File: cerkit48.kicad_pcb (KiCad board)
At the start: 2 copper layers, 237.3 x 84.9 mm, 103 parts, among them J1 I2C, SW10 CherryMX, SW11 CherryMX, SW12 CherryMX, SW13 CherryMX, SW14 CherryMX, SW15 CherryMX, SW16 CherryMX, SW17 CherryMX, SW18 CherryMX, SW19 CherryMX, SW2 CherryMX, SW20 CherryMX, SW21 CherryMX, SW22 CherryMX, SW23 CherryMX, SW24 CherryMX, SW25 CherryMX, SW26 CherryMX, SW27 CherryMX, SW28 CherryMX, SW29 CherryMX, SW3 CherryMX, SW30 CherryMX, SW31 CherryMX, SW32 CherryMX, SW33 CherryMX, SW34 CherryMX, SW35 CherryMX, SW36 CherryMX, SW37 CherryMX, SW38 CherryMX, SW39 CherryMX, SW4 CherryMX, SW40 CherryMX, SW41 CherryMX, SW42 CherryMX, SW43 CherryMX, SW44 CherryMX, SW45 CherryMX, SW46 CherryMX, SW47 CherryMX, SW48 CherryMX, SW49 CherryMX, SW5 CherryMX, SW6 CherryMX, SW7 CherryMX, SW8 CherryMX, SW9 CherryMX, U1 proton_c

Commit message: rounded the edges of the board
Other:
- board size 237.3 x 84.9 mm -> 235.7 x 83.3 mm

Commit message: rounded the edges of the PCB
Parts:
- moved J1 0.48 mm to (208.3, 54.5)
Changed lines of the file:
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@@
   (layers
     (0 F.Cu signal)
-    (31 B.Cu signal)
+    (31 B.Cu signal hide)
     (32 B.Adhes user hide)
     (33 F.Adhes user hide)
@@
     (35 F.Paste user hide)
     (36 B.SilkS user hide)
-    (37 F.SilkS user hide)
+    (37 F.SilkS user)
     (38 B.Mask user hide)
     (39 F.Mask user hide)
@@
   )
   (module cerkit48:PIN_HEADER_I2C (layer F.Cu)
-    (at 208.28 53.975 270)
+    (at 208.28 54.45125 270)
     (fp_text reference J1 (at 0 0.5 90) (layer F.SilkS)
       (effects (font (size 1 1) (thickness 0.15)))
@@
     (polygon
       (pts
-        (xy 259.55625 134.9375) (xy 23.8125 134.9375) (xy 23.8125 51.59375) (xy 259.55625 50.8)
+        (xy 259.55625 134.9375) (xy 23.8125 134.9375) (xy 23.8125 51.59375) (xy 259.55625 51.59375)
       )
     )

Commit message: modified gerber files
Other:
- net class Default: trace_width 0.25 -> 0.254
- net class Power added: clearance 0.2, trace_width 0.381, via_dia 0.8, via_drill 0.4
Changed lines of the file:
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@@
     (thickness 1.6)
     (drawings 92)
-    (tracks 384)
+    (tracks 385)
     (zones 0)
     (modules 103)
@@
   (layers
     (0 F.Cu signal)
-    (31 B.Cu signal hide)
+    (31 B.Cu signal)
     (32 B.Adhes user hide)
     (33 F.Adhes user hide)
@@
   )
   (setup
-    (last_trace_width 0.25)
+    (last_trace_width 0.254)
     (trace_clearance 0.2)
     (zone_clearance 0.508)
@@
   (net_class Default "This is the default net class."
     (clearance 0.2)
-    (trace_width 0.25)
+    (trace_width 0.254)
     (via_dia 0.8)
     (via_drill 0.4)
     (uvia_dia 0.3)
     (uvia_drill 0.1)
-    (add_net 3.3V)
     (add_net COL0)
     (add_net COL1)
@@
     (add_net COL8)
     (add_net COL9)
-    (add_net GND)
     (add_net "Net-(D1-Pad2)")
     (add_net "Net-(D10-Pad2)")
@@
     (add_net SDA)
   )
+  (net_class Power ""
+    (clearance 0.2)
+    (trace_width 0.381)
+    (via_dia 0.8)
+    (via_drill 0.4)
+    (uvia_dia 0.3)
+    (uvia_drill 0.1)
+    (add_net 3.3V)
+    (add_net GND)
+  )
   (module MountingHole:MountingHole_3.2mm_M3 (layer F.Cu)
     (at 256.54 54.61 180)
@@
   (segment (start 199.920001 111.020001) (end 199.920001 53.444999) (width 0.25) (layer B.Cu) (net 54))
   (segment (start 202.565 113.665) (end 199.920001 111.020001) (width 0.25) (layer B.Cu) (net 54))
-  (segment (start 202.460001 101.833997) (end 201.422 102.871998) (width 0.25) (layer B.Cu) (net 55))
-  (segment (start 202.460001 94.705999) (end 202.460001 101.833997) (width 0.25) (layer B.Cu) (net 55))
-  (segment (start 201.682499 93.928497) (end 202.460001 94.705999) (width 0.25) (layer B.Cu) (net 55))
-  (segment (start 203.2 52.705) (end 201.682499 54.222501) (width 0.25) (layer B.Cu) (net 55))
-  (segment (start 201.682499 54.222501) (end 201.682499 93.928497) (width 0.25) (layer B.Cu) (net 55))
-  (segment (start 201.422 102.871998) (end 201.422 107.442) (width 0.25) (layer B.Cu) (net 55))
   (segment (start 201.422 107.442) (end 201.422 107.442) (width 0.25) (layer B.Cu) (net 55))
   (via (at 201.422 107.442) (size 0.8) (drill 0.4) (layers F.Cu B.Cu) (net 55))
   (segment (start 203.322 107.442) (end 206.365 110.485) (width 0.25) (layer F.Cu) (net 55))
   (segment (start 201.422 107.442) (end 203.322 107.442) (width 0.25) (layer F.Cu) (net 55))
+  (segment (start 202.525501 94.674559) (end 202.525501 95.924499) (width 0.381) (layer B.Cu) (net 55))
+  (segment (start 201.616999 93.766057) (end 202.525501 94.674559) (width 0.381) (layer B.Cu) (net 55))
+  (segment (start 203.2 53.18125) (end 201.616999 54.764251) (width 0.381) (layer B.Cu) (net 55))
+  (segment (start 201.616999 54.764251) (end 201.616999 93.766057) (width 0.381) (layer B.Cu) (net 55))
+  (segment (start 201.616999 107.247001) (end 201.422 107.442) (width 0.381) (layer B.Cu) (net 55))
+  (segment (start 201.616999 96.833001) (end 201.616999 107.247001) (width 0.381) (layer B.Cu) (net 55))
+  (segment (start 202.525501 95.924499) (end 201.616999 96.833001) (width 0.381) (layer B.Cu) (net 55))
   (segment (start 206.365 95.24) (end 206.375 95.25) (width 0.25) (layer B.Cu) (net 56))
   (segment (start 32.749463 81.75035) (end 32.870936 81.871823) (width 0.25) (layer B.Cu) (net 57))
@@
   (segment (start 242.2525 100.6475) (end 243.100001 101.495001) (width 0.25) (layer B.Cu) (net 68))
   (segment (start 231.765 95.24) (end 231.775 95.25) (width 0.25) (layer F.Cu) (net 73))
-  (zone (net 56) (net_name GND) (layer F.Cu) (hatch edge 0.508)
+  (zone (net 56) (net_name GND) (layer B.Cu) (hatch edge 0.508)
     (connect_pads (clearance 0.508))
     (min_thickness 0.254)
@@
     )
   )
-  (zone (net 56) (net_name GND) (layer B.Cu) (hatch edge 0.508)
+  (zone (net 56) (net_name GND) (layer F.Cu) (hatch edge 0.508)
     (connect_pads (clearance 0.508))
     (min_thickness 0.254)

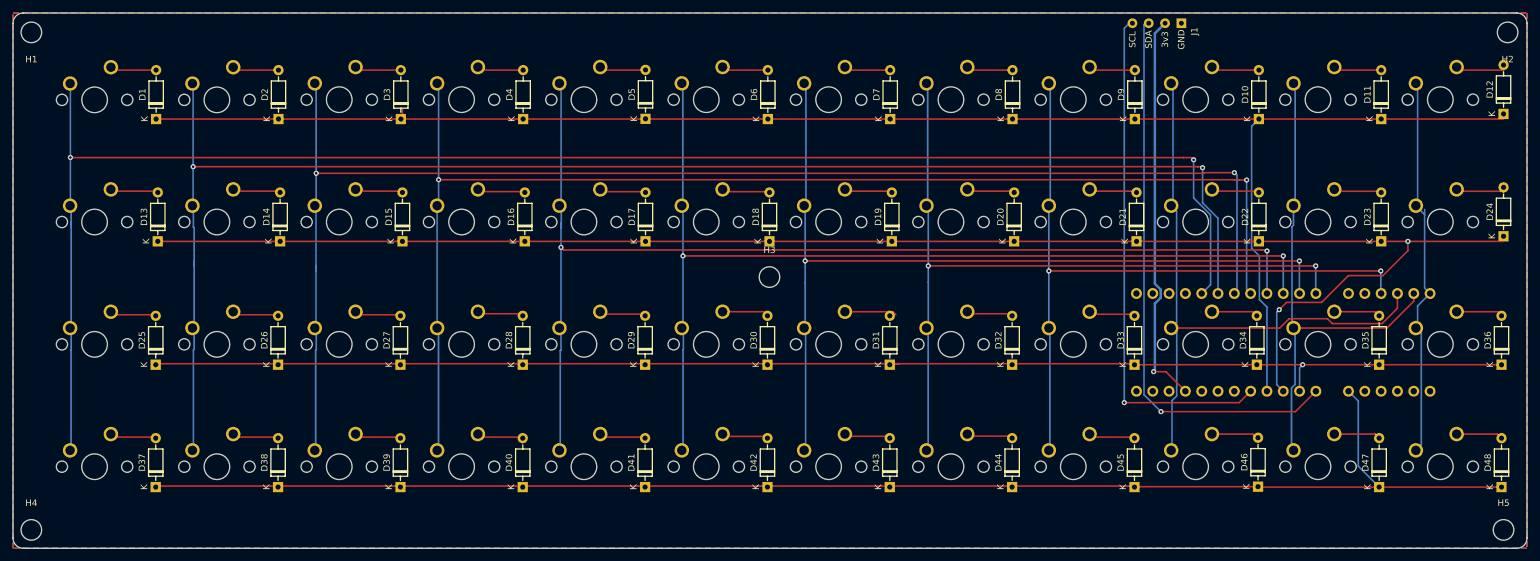
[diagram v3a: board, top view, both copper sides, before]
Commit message: fixed PCB outline
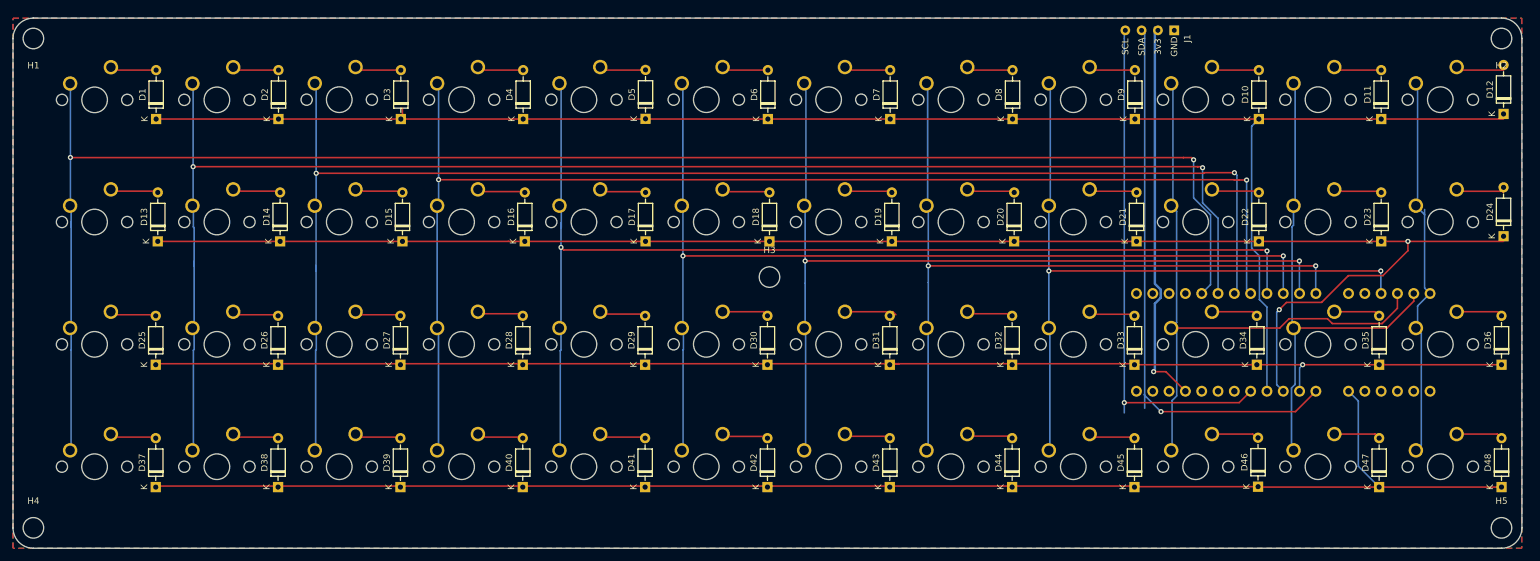
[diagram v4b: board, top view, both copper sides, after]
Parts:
- moved J1 1.57 mm to (207.2, 55.6)
- moved H2 1.35 mm to (255.6, 55.6)
- moved H1 1.00 mm to (27.0, 55.6)
- moved H4 0.45 mm to (27.0, 131.8)
- moved H5 0.45 mm to (255.6, 131.8)
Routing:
- net 3.3V: track 62.0 -> 61.2 mm
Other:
- board size 235.7 x 83.3 mm -> 235 x 82.5 mm

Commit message: centered middle mounting hole
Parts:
- moved D12 1.00 mm to (255.6, 68.3)
- moved H3 1.00 mm to (141.3, 93.7)
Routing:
- net SDA: track 88.2 -> 86.1 mm
- net SCL: track 80.0 -> 78.5 mm
- net 3.3V: track 61.2 -> 62.6 mm
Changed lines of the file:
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@@
     (thickness 1.6)
     (drawings 8)
-    (tracks 387)
+    (tracks 390)
     (zones 0)
     (modules 103)
@@
     (35 F.Paste user hide)
     (36 B.SilkS user)
-    (37 F.SilkS user)
-    (38 B.Mask user)
+    (37 F.SilkS user hide)
+    (38 B.Mask user hide)
     (39 F.Mask user)
     (40 Dwgs.User user)
@@
     (45 Margin user hide)
     (46 B.CrtYd user hide)
-    (47 F.CrtYd user hide)
+    (47 F.CrtYd user)
     (48 B.Fab user hide)
     (49 F.Fab user hide)
@@
   )
   (module Diode_THT:D_DO-35_SOD27_P7.62mm_Horizontal (layer F.Cu)
-    (at 255.905 67.31 90)
+    (at 255.5875 68.2625 90)
     (descr "Diode, DO-35_SOD27 series, Axial, Horizontal, pin pitch=7.62mm, , length*diameter=4*2mm^2, , http://www.diodes.com/_files/packages/DO-35.pdf")
     (tags "Diode DO-35_SOD27 series Axial Horizontal pin pitch 7.62mm  length 4mm diameter 2mm")
@@
   )
   (module MountingHole:MountingHole_3.2mm_M3 (layer F.Cu)
-    (at 141.605 92.71)
+    (at 141.2875 93.6625)
     (descr "Mounting Hole 3.2mm, no annular, M3")
     (tags "mounting hole 3.2mm no annular m3")
@@
   (segment (start 198.755 68.10375) (end 217.805 68.10375) (width 0.25) (layer F.Cu) (net 2))
   (segment (start 217.805 68.10375) (end 236.855 68.10375) (width 0.25) (layer F.Cu) (net 2))
-  (segment (start 236.855 68.10375) (end 255.905 68.10375) (width 0.25) (layer F.Cu) (net 2))
   (segment (start 84.455 68.10375) (end 84.455 66.475652) (width 0.25) (layer F.Cu) (net 2))
   (segment (start 219.065 97.384998) (end 219.065 110.485) (width 0.25) (layer B.Cu) (net 2))
@@
   (segment (start 216.679999 69.228751) (end 216.679999 88.213751) (width 0.25) (layer B.Cu) (net 2))
   (segment (start 217.805 68.10375) (end 216.679999 69.228751) (width 0.25) (layer B.Cu) (net 2))
+  (segment (start 255.42875 68.10375) (end 255.5875 68.2625) (width 0.254) (layer F.Cu) (net 2))
+  (segment (start 236.855 68.10375) (end 255.42875 68.10375) (width 0.254) (layer F.Cu) (net 2))
   (segment (start 58.296875 60.48375) (end 58.208345 60.39522) (width 0.25) (layer F.Cu) (net 3))
   (segment (start 65.405 60.48375) (end 58.296875 60.48375) (width 0.25) (layer F.Cu) (net 3))
@@
   (segment (start 229.91352 60.48375) (end 229.806152 60.376382) (width 0.25) (layer F.Cu) (net 12))
   (segment (start 236.855 60.48375) (end 229.91352 60.48375) (width 0.25) (layer F.Cu) (net 12))
-  (segment (start 255.905 60.48375) (end 249.026559 60.48375) (width 0.25) (layer F.Cu) (net 13))
+  (segment (start 254.9525 60.0075) (end 255.5875 60.6425) (width 0.254) (layer F.Cu) (net 13))
+  (segment (start 248.6025 60.0075) (end 254.9525 60.0075) (width 0.254) (layer F.Cu) (net 13))
   (segment (start 46.153073 79.331823) (end 46.355 79.53375) (width 0.25) (layer F.Cu) (net 14))
   (segment (start 39.220936 79.331823) (end 46.153073 79.331823) (width 0.25) (layer F.Cu) (net 14))
@@
   (segment (start 216.525 110.485) (end 214.742 112.268) (width 0.25) (layer F.Cu) (net 53))
   (segment (start 214.742 112.268) (end 196.85 112.268) (width 0.25) (layer F.Cu) (net 53))
-  (segment (start 196.85 113.8555) (end 196.85 55.5625) (width 0.25) (layer B.Cu) (net 53))
   (via (at 196.85 112.268) (size 0.8) (drill 0.4) (layers F.Cu B.Cu) (net 53))
-  (segment (start 196.85 54.45125) (end 197.00875 54.2925) (width 0.254) (layer B.Cu) (net 53))
-  (segment (start 196.85 55.5625) (end 196.85 54.45125) (width 0.254) (layer B.Cu) (net 53))
-  (via (at 202.565 113.665) (size 0.8) (drill 0.4) (layers F.Cu B.Cu) (net 54))
-  (segment (start 223.505 113.665) (end 226.685 110.485) (width 0.25) (layer F.Cu) (net 54))
+  (segment (start 197.00875 112.10925) (end 196.85 112.268) (width 0.254) (layer B.Cu) (net 53))
+  (segment (start 197.00875 54.2925) (end 197.00875 112.10925) (width 0.254) (layer B.Cu) (net 53))
   (segment (start 202.565 113.665) (end 223.505 113.665) (width 0.25) (layer F.Cu) (net 54))
-  (segment (start 200.025 113.137502) (end 200.025 55.5625) (width 0.25) (layer B.Cu) (net 54))
-  (segment (start 202.565 113.665) (end 199.920001 111.020001) (width 0.25) (layer B.Cu) (net 54))
-  (segment (start 200.025 54.76875) (end 199.54875 54.2925) (width 0.254) (layer B.Cu) (net 54))
-  (segment (start 200.025 55.5625) (end 200.025 54.76875) (width 0.254) (layer B.Cu) (net 54))
+  (segment (start 223.505 113.665) (end 226.685 110.485) (width 0.25) (layer F.Cu) (net 54))
+  (via (at 202.565 113.665) (size 0.8) (drill 0.4) (layers F.Cu B.Cu) (net 54))
+  (segment (start 199.922001 54.665751) (end 199.922001 111.022001) (width 0.254) (layer B.Cu) (net 54))
+  (segment (start 199.54875 54.2925) (end 199.922001 54.665751) (width 0.254) (layer B.Cu) (net 54))
+  (segment (start 199.922001 111.022001) (end 202.40625 113.50625) (width 0.254) (layer B.Cu) (net 54))
+  (segment (start 202.40625 113.50625) (end 202.565 113.665) (width 0.254) (layer B.Cu) (net 54))
   (segment (start 201.422 107.442) (end 201.422 107.442) (width 0.25) (layer B.Cu) (net 55))
   (via (at 201.422 107.442) (size 0.8) (drill 0.4) (layers F.Cu B.Cu) (net 55))
   (segment (start 203.322 107.442) (end 206.365 110.485) (width 0.25) (layer F.Cu) (net 55))
   (segment (start 201.422 107.442) (end 203.322 107.442) (width 0.25) (layer F.Cu) (net 55))
-  (segment (start 202.525501 94.674559) (end 202.525501 95.924499) (width 0.381) (layer B.Cu) (net 55))
   (segment (start 201.616999 93.766057) (end 202.525501 94.674559) (width 0.381) (layer B.Cu) (net 55))
-  (segment (start 201.616999 107.247001) (end 201.422 107.442) (width 0.381) (layer B.Cu) (net 55))
-  (segment (start 201.616999 96.833001) (end 201.616999 107.247001) (width 0.381) (layer B.Cu) (net 55))
-  (segment (start 202.525501 95.924499) (end 201.616999 96.833001) (width 0.381) (layer B.Cu) (net 55))
   (segment (start 201.616999 54.764251) (end 202.08875 54.2925) (width 0.381) (layer B.Cu) (net 55))
-  (segment (start 201.6125 93.6625) (end 201.6125 53.862445) (width 0.381) (layer B.Cu) (net 55))
+  (segment (start 201.616999 107.247001) (end 201.422 107.442) (width 0.381) (layer B.Cu) (net 55))
+  (segment (start 201.616999 102.627753) (end 201.616999 107.247001) (width 0.381) (layer B.Cu) (net 55))
+  (segment (start 202.525501 101.719251) (end 201.616999 102.627753) (width 0.381) (layer B.Cu) (net 55))
+  (segment (start 201.326751 93.475809) (end 202.525501 94.674559) (width 0.381) (layer B.Cu) (net 55))
+  (segment (start 202.525501 94.674559) (end 202.525501 101.719251) (width 0.381) (layer B.Cu) (net 55))
+  (segment (start 201.326751 55.054499) (end 201.326751 93.475809) (width 0.381) (layer B.Cu) (net 55))
+  (segment (start 202.08875 54.2925) (end 201.326751 55.054499) (width 0.381) (layer B.Cu) (net 55))
   (segment (start 206.365 95.24) (end 206.375 95.25) (width 0.25) (layer B.Cu) (net 56))
   (segment (start 32.749463 81.75035) (end 32.870936 81.871823) (width 0.25) (layer B.Cu) (net 57))

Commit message: reset switch number annotations
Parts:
- renumbered SW2 to SW1, SW11 to SW10, SW12 to SW11, SW13 to SW12, SW14 to SW13, SW15 to SW14, SW16 to SW15, SW17 to SW16, SW18 to SW17, SW19 to SW18, SW20 to SW19, SW3 to SW2, SW21 to SW20, SW22 to SW21, SW23 to SW22, SW24 to SW23, SW25 to SW24, SW26 to SW25, SW27 to SW26, SW28 to SW27, SW29 to SW28, SW30 to SW29, SW4 to SW3, SW31 to SW30, SW32 to SW31, SW33 to SW32, SW34 to SW33, SW35 to SW34, SW36 to SW35, SW37 to SW36, SW38 to SW37, SW39 to SW38, SW40 to SW39, SW5 to SW4, SW41 to SW40, SW42 to SW41, SW43 to SW42, SW44 to SW43, SW45 to SW44, SW46 to SW45, SW47 to SW46, SW48 to SW47, SW49 to SW48, SW6 to SW5, SW7 to SW6, SW8 to SW7, SW9 to SW8, SW10 to SW9

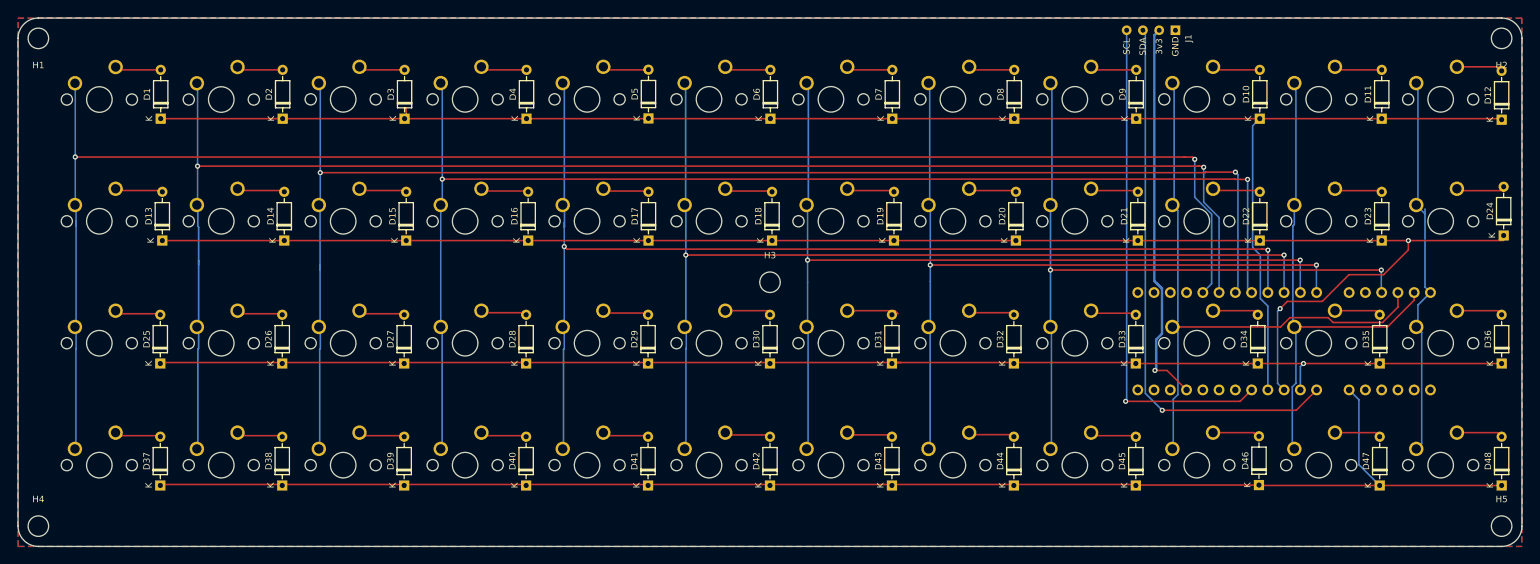
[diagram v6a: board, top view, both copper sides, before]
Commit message: adjusted outline so that standoffs would fit
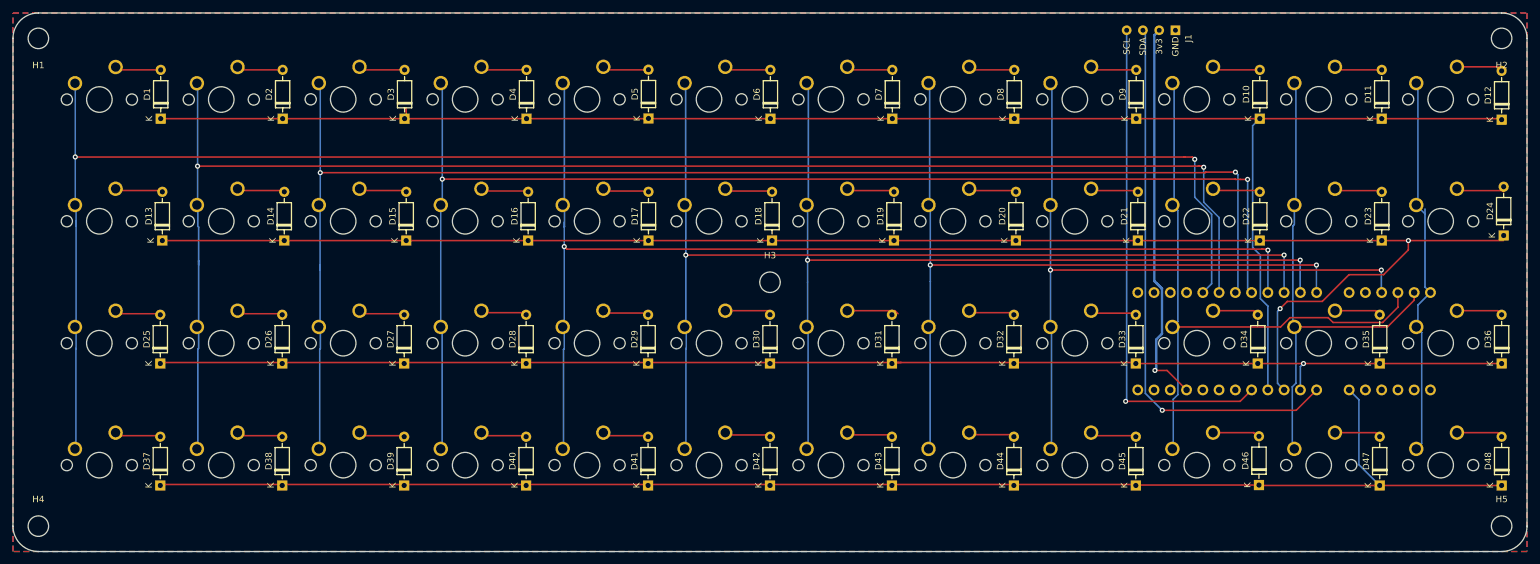
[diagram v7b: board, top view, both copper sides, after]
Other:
- board size 235 x 82.5 mm -> 236.5 x 84.1 mm
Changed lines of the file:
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@@
   (layers
     (0 F.Cu signal)
-    (31 B.Cu signal hide)
+    (31 B.Cu signal)
     (32 B.Adhes user hide)
     (33 F.Adhes user hide)
     (34 B.Paste user hide)
     (35 F.Paste user hide)
-    (36 B.SilkS user)
+    (36 B.SilkS user hide)
     (37 F.SilkS user hide)
     (38 B.Mask user hide)
-    (39 F.Mask user)
+    (39 F.Mask user hide)
     (40 Dwgs.User user)
     (41 Cmts.User user hide)
@@
     (pad 1 np_thru_hole circle (at 0 0 180) (size 3.2 3.2) (drill 3.2) (layers *.Cu *.Mask))
   )
-  (gr_line (start 26.9875 52.3875) (end 255.5875 52.3875) (layer Edge.Cuts) (width 0.05))
-  (gr_line (start 23.8125 131.7625) (end 23.8125 55.5625) (layer Edge.Cuts) (width 0.05))
-  (gr_line (start 255.5875 134.9375) (end 26.9875 134.9375) (layer Edge.Cuts) (width 0.05))
-  (gr_line (start 258.7625 55.5625) (end 258.7625 131.7625) (layer Edge.Cuts) (width 0.05))
-  (gr_arc (start 255.5875 55.5625) (end 258.7625 55.5625) (angle -90) (layer Edge.Cuts) (width 0.05))
-  (gr_arc (start 255.5875 131.7625) (end 255.5875 134.9375) (angle -90) (layer Edge.Cuts) (width 0.05))
-  (gr_arc (start 26.9875 131.7625) (end 23.8125 131.7625) (angle -90) (layer Edge.Cuts) (width 0.05))
-  (gr_arc (start 26.9875 55.5625) (end 26.9875 52.3875) (angle -90) (layer Edge.Cuts) (width 0.05))
+  (gr_line (start 26.9875 51.59375) (end 255.5875 51.59375) (layer Edge.Cuts) (width 0.05))
+  (gr_line (start 23.01875 131.7625) (end 23.01875 55.5625) (layer Edge.Cuts) (width 0.05))
+  (gr_line (start 255.5875 135.73125) (end 26.9875 135.73125) (layer Edge.Cuts) (width 0.05))
+  (gr_line (start 259.55625 55.5625) (end 259.55625 131.7625) (layer Edge.Cuts) (width 0.05))
+  (gr_arc (start 255.5875 55.5625) (end 259.55625 55.5625) (angle -90) (layer Edge.Cuts) (width 0.05))
+  (gr_arc (start 255.5875 131.7625) (end 255.5875 135.73125) (angle -90) (layer Edge.Cuts) (width 0.05))
+  (gr_arc (start 26.9875 131.7625) (end 23.01875 131.7625) (angle -90) (layer Edge.Cuts) (width 0.05))
+  (gr_arc (start 26.9875 55.5625) (end 26.9875 51.59375) (angle -90) (layer Edge.Cuts) (width 0.05))
   (segment (start 39.142767 60.48375) (end 39.099463 60.440446) (width 0.25) (layer F.Cu) (net 1))
   (segment (start 46.355 60.48375) (end 39.142767 60.48375) (width 0.25) (layer F.Cu) (net 1))
@@
     (polygon
       (pts
-        (xy 258.7625 134.9375) (xy 23.8125 134.9375) (xy 23.8125 52.3875) (xy 258.7625 52.3875)
+        (xy 259.55625 135.73125) (xy 23.01875 135.73125) (xy 23.01875 51.59375) (xy 259.55625 51.59375)
       )
     )
@@
     (polygon
       (pts
-        (xy 258.7625 134.9375) (xy 23.8125 134.9375) (xy 23.8125 52.3875) (xy 258.7625 52.3875)
+        (xy 259.55625 135.73125) (xy 23.01875 135.73125) (xy 23.01875 51.59375) (xy 259.55625 51.59375)
       )
     )
